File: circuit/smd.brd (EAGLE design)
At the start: 37.8 x 17.8 mm, 16 parts, among them IC1 AT90S2313S, Q1 16MHz, X1 USB-1X-2S-PLUG-A-THT

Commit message: further refinements
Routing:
- net +5V: track 80.6 -> 78.8 mm
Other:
- board text added: "1"
- board text added: "ISP"
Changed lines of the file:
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@@
 <text x="34.29" y="15.875" size="1.016" layer="25">5V</text>
 <text x="34.29" y="1.27" size="1.016" layer="25">GND</text>
+<text x="24.765" y="12.7" size="1.016" layer="25">1</text>
+<text x="26.035" y="5.08" size="1.016" layer="25" rot="R180">ISP</text>
 </plain>
 <attributes>
@@
 </element>
 <element name="R6" library="rcl" package="R0805" value="68R" x="16.51" y="8.89" smashed="yes" rot="MR180">
-<attribute name="NAME" x="19.812" y="8.001" size="0.8128" layer="26" ratio="10" rot="MR180"/>
+<attribute name="NAME" x="12.827" y="9.271" size="0.8128" layer="26" ratio="10" rot="MR180"/>
 <attribute name="VALUE" x="14.2494" y="9.525" size="1.27" layer="28" ratio="10" rot="MR180"/>
 </element>
 <element name="R4" library="rcl" package="R0805" value="68R" x="16.51" y="11.43" smashed="yes" rot="MR180">
-<attribute name="NAME" x="19.812" y="10.541" size="0.8128" layer="26" ratio="10" rot="MR180"/>
+<attribute name="NAME" x="12.827" y="11.811" size="0.8128" layer="26" ratio="10" rot="MR180"/>
 <attribute name="VALUE" x="14.2494" y="12.065" size="1.27" layer="28" ratio="10" rot="MR180"/>
 </element>
@@
 <wire x1="31.75" y1="11.43" x2="33.02" y2="12.7" width="0.4064" layer="1"/>
 <wire x1="33.02" y1="12.7" x2="34.925" y2="12.7" width="0.4064" layer="1"/>
-<wire x1="28.89" y1="3.175" x2="32.385" y2="3.175" width="0.4064" layer="1"/>
-<via x="32.385" y="3.175" extent="1-16" drill="0.7"/>
-<wire x1="32.385" y1="3.175" x2="32.385" y2="5.08" width="0.4064" layer="16"/>
-<wire x1="32.385" y1="5.08" x2="31.115" y2="6.35" width="0.4064" layer="16"/>
+<wire x1="28.89" y1="3.175" x2="31.115" y2="3.175" width="0.4064" layer="1"/>
+<via x="31.115" y="3.175" extent="1-16" drill="0.7"/>
+<wire x1="31.115" y1="3.175" x2="31.115" y2="6.35" width="0.4064" layer="16"/>
 <via x="31.115" y="6.35" extent="1-16" drill="0.7"/>
 <wire x1="31.115" y1="6.35" x2="31.115" y2="9.525" width="0.4064" layer="1"/>

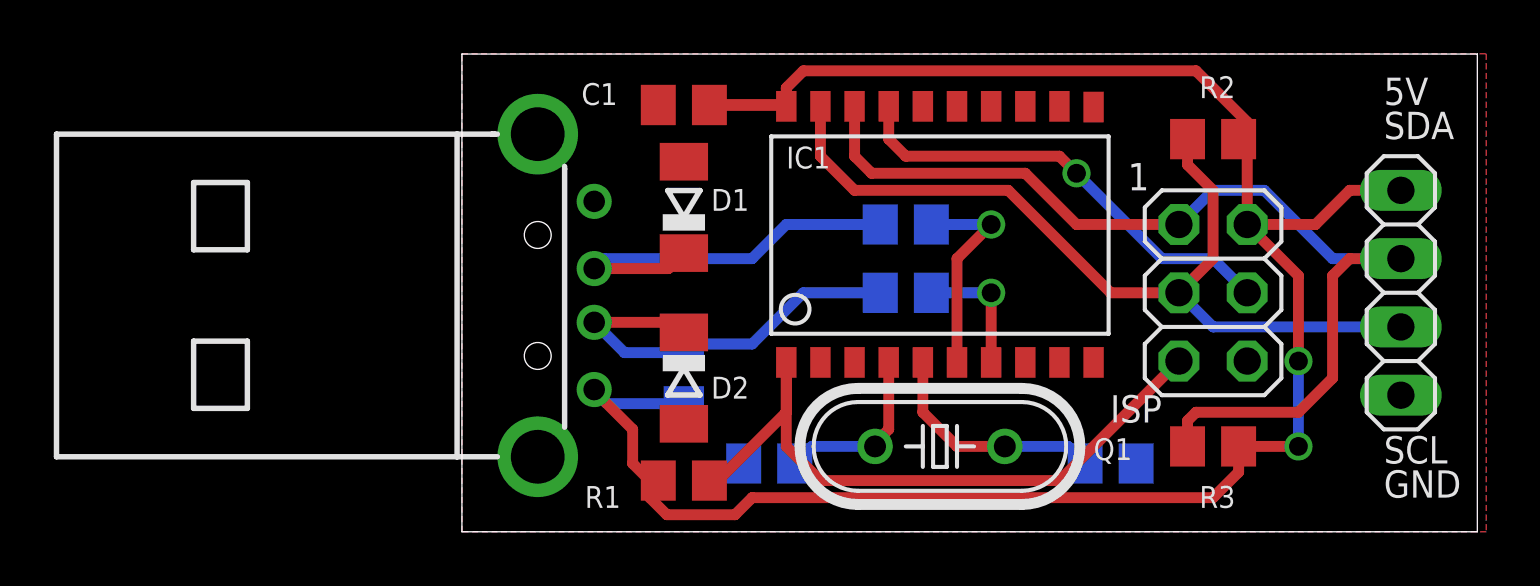
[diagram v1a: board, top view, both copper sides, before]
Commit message: smd layout: add status LEDs, cause status LEDs are always good \o/
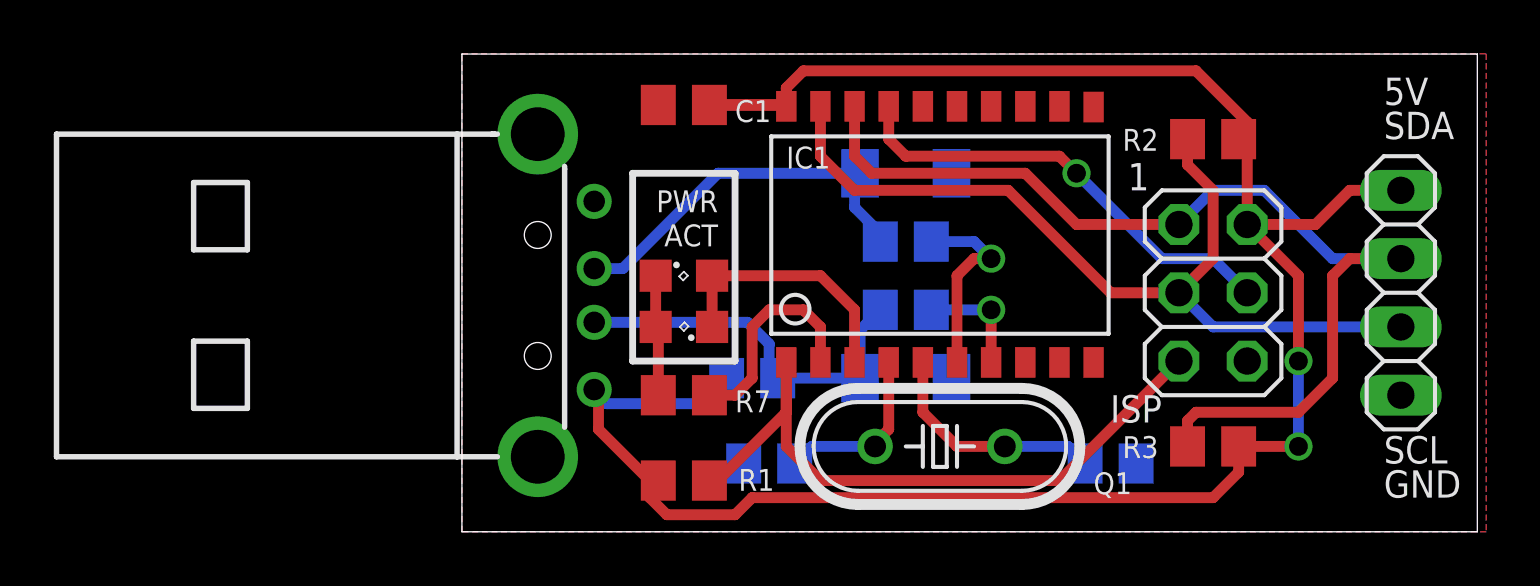
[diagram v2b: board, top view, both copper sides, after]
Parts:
- added LED1, LED2: (no value), led:SML0805
- added R7: (no value), rcl:R0805
- moved D1 8.35 mm to (16.5, 13.3), flipped to the bottom, turned to 180 degrees
- moved D2 8.26 mm to (16.5, 5.71), flipped to the bottom, turned to 180 degrees
- moved R5 2.54 mm to (10.8, 5.71), turned to 0 degrees
- moved R4 0.63 mm to (16.5, 10.8)
- moved R6 0.63 mm to (16.5, 8.26)
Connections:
- new net LED1: IC1.3, LED1.C, LED2.A
- new net LED2: IC1.2, R7.1
- new net N$2: LED1.A, LED2.C, R7.2
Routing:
- net LED1: track 0.00 -> 9.69 mm
- net LED2: track 0.00 -> 8.14 mm
- net N$2: track 0.00 -> 4.49 mm
- net +5V: track 78.8 -> 80.8 mm
- net D-: track 15.5 -> 14.2 mm
- net AVRD-: track 4.82 -> 4.18 mm
- net AVRD+: track 7.88 -> 7.25 mm
- net D+: track 14.9 -> 14.4 mm
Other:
- board text added: "ACT"
- board text added: "PWR"

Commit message: smd rev 1 at board house
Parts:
- LED1: value (none) -> act
- LED2: value (none) -> pwr
- R7: value (none) -> 150..1K
- moved LED1 1.27 mm to (8.26, 8.89)
- moved LED2 1.27 mm to (8.26, 10.8)
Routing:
- net N$2: track 4.49 -> 5.81 mm
- net LED1: track 9.69 -> 10.2 mm
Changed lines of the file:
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@@
 <text x="26.035" y="5.08" size="1.016" layer="25" rot="R180">ISP</text>
 <text x="9.525" y="12.7" size="0.8128" layer="25" rot="R180">PWR</text>
-<text x="9.525" y="11.43" size="0.8128" layer="25" rot="R180">ACT</text>
+<text x="9.525" y="7.62" size="0.8128" layer="25" rot="R180">ACT</text>
 <wire x1="6.35" y1="6.35" x2="10.16" y2="6.35" width="0.254" layer="25"/>
 <wire x1="10.16" y1="6.35" x2="10.16" y2="13.335" width="0.254" layer="25"/>
@@
 </class>
 </classes>
-<designrules name="dirtypcbs_v1">
+<designrules name="dirtypcbs_v1 *">
 <description language="en">&lt;b&gt;Dirty Cheap Dirty Board Design Rules&lt;/b&gt;
 &lt;br&gt;
@@
 <param name="dpGapFactor" value="2.5"/>
 <param name="checkGrid" value="0"/>
-<param name="checkAngle" value="0"/>
+<param name="checkAngle" value="1"/>
 <param name="checkFont" value="1"/>
-<param name="checkRestrict" value="0"/>
+<param name="checkRestrict" value="1"/>
 <param name="useDiameter" value="13"/>
 <param name="maxErrors" value="50"/>
@@
 </element>
 <element name="C2" library="rcl" package="C0805" value="22p" x="11.43" y="2.54" smashed="yes" rot="MR180">
-<attribute name="NAME" x="12.065" y="3.81" size="0.8128" layer="26" rot="MR0"/>
+<attribute name="NAME" x="7.62" y="3.175" size="0.8128" layer="26" rot="MR180"/>
 <attribute name="VALUE" x="10.16" y="5.08" size="1.27" layer="28" rot="MR180"/>
 </element>
 <element name="R5" library="rcl" package="R0805" value="1k5" x="10.795" y="5.715" smashed="yes" rot="MR0">
-<attribute name="NAME" x="11.176" y="4.318" size="0.8128" layer="26" ratio="10" rot="MR270"/>
+<attribute name="NAME" x="7.112" y="6.096" size="0.8128" layer="26" ratio="10" rot="MR180"/>
 <attribute name="VALUE" x="13.0556" y="5.08" size="1.27" layer="28" ratio="10" rot="MR0"/>
 </element>
@@
 </element>
 <element name="D2" library="diode" package="SOD80C" value="3V3" x="16.51" y="5.715" smashed="yes" rot="MR180">
-<attribute name="NAME" x="17.272" y="4.699" size="0.8128" layer="26" ratio="10" rot="MR270"/>
+<attribute name="NAME" x="13.081" y="4.572" size="0.8128" layer="26" ratio="10" rot="MR180"/>
 <attribute name="VALUE" x="14.986" y="8.128" size="1.27" layer="28" ratio="10" rot="MR180"/>
 </element>
 <element name="D1" library="diode" package="SOD80C" value="3V3" x="16.51" y="13.335" smashed="yes" rot="MR180">
-<attribute name="NAME" x="16.383" y="14.351" size="0.8128" layer="26" ratio="10" rot="MR90"/>
+<attribute name="NAME" x="12.446" y="14.097" size="0.8128" layer="26" ratio="10" rot="MR180"/>
 <attribute name="VALUE" x="14.986" y="15.748" size="1.27" layer="28" ratio="10" rot="MR180"/>
 </element>
@@
 <attribute name="VALUE" x="4.42" y="2.89" size="1.27" layer="27"/>
 </element>
-<element name="LED1" library="led" package="SML0805" value="" x="8.255" y="7.62" smashed="yes" rot="R180">
-<attribute name="NAME" x="9.755" y="6.62" size="1.27" layer="27" rot="R180"/>
-<attribute name="VALUE" x="9.755" y="9.62" size="1.27" layer="27" rot="R180"/>
-</element>
-<element name="LED2" library="led" package="SML0805" value="" x="8.255" y="9.525" smashed="yes">
-<attribute name="NAME" x="6.755" y="10.525" size="1.27" layer="27"/>
-<attribute name="VALUE" x="6.755" y="7.525" size="1.27" layer="27"/>
-</element>
-<element name="R7" library="rcl" package="R0805" value="" x="8.255" y="5.08" smashed="yes" rot="R180">
+<element name="LED1" library="led" package="SML0805" value="act" x="8.255" y="8.89" smashed="yes" rot="R180">
+<attribute name="NAME" x="9.755" y="7.89" size="1.27" layer="27" rot="R180"/>
+<attribute name="VALUE" x="9.755" y="10.89" size="1.27" layer="27" rot="R180"/>
+</element>
+<element name="LED2" library="led" package="SML0805" value="pwr" x="8.255" y="10.795" smashed="yes">
+<attribute name="NAME" x="6.755" y="11.795" size="1.27" layer="27"/>
+<attribute name="VALUE" x="6.755" y="8.795" size="1.27" layer="27"/>
+</element>
+<element name="R7" library="rcl" package="R0805" value="150..1K" x="8.255" y="5.08" smashed="yes" rot="R180">
 <attribute name="NAME" x="10.16" y="4.445" size="0.8128" layer="25"/>
 <attribute name="VALUE" x="8.89" y="7.62" size="1.27" layer="27" rot="R180"/>
@@
 <contactref element="LED1" pad="C"/>
 <contactref element="LED2" pad="A"/>
-<wire x1="9.305" y1="9.525" x2="9.305" y2="7.62" width="0.4064" layer="1"/>
+<wire x1="9.305" y1="10.795" x2="9.305" y2="8.89" width="0.4064" layer="1"/>
 <wire x1="14.605" y1="6.2992" x2="14.605" y2="8.255" width="0.4064" layer="1"/>
-<wire x1="14.605" y1="8.255" x2="13.335" y2="9.525" width="0.4064" layer="1"/>
-<wire x1="13.335" y1="9.525" x2="9.305" y2="9.525" width="0.4064" layer="1"/>
+<wire x1="14.605" y1="8.255" x2="12.065" y2="10.795" width="0.4064" layer="1"/>
+<wire x1="12.065" y1="10.795" x2="9.305" y2="10.795" width="0.4064" layer="1"/>
 </signal>
 <signal name="N$2">
@@
 <contactref element="LED1" pad="A"/>
 <contactref element="LED2" pad="C"/>
-<wire x1="7.305" y1="5.08" x2="7.305" y2="7.52" width="0.4064" layer="1"/>
-<wire x1="7.305" y1="7.52" x2="7.205" y2="7.62" width="0.4064" layer="1"/>
-<wire x1="7.205" y1="7.62" x2="7.205" y2="9.525" width="0.4064" layer="1"/>
+<wire x1="7.205" y1="8.89" x2="7.205" y2="10.795" width="0.4064" layer="1"/>
+<wire x1="7.305" y1="5.08" x2="7.205" y2="5.08" width="0.4064" layer="1"/>
+<wire x1="7.205" y1="5.08" x2="7.205" y2="8.89" width="0.4064" layer="1"/>
 </signal>
 </signals>
